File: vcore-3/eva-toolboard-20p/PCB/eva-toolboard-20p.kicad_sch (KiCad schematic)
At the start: 10 parts, among them J1 TH0, J2 HEATER, J3 STEPPER, J4 Main connector, J5 HOTENDFAN, J6 PARTFAN_1, J7 PARTFAN_2, J8 ENDSTOP_X, J9 PROBE

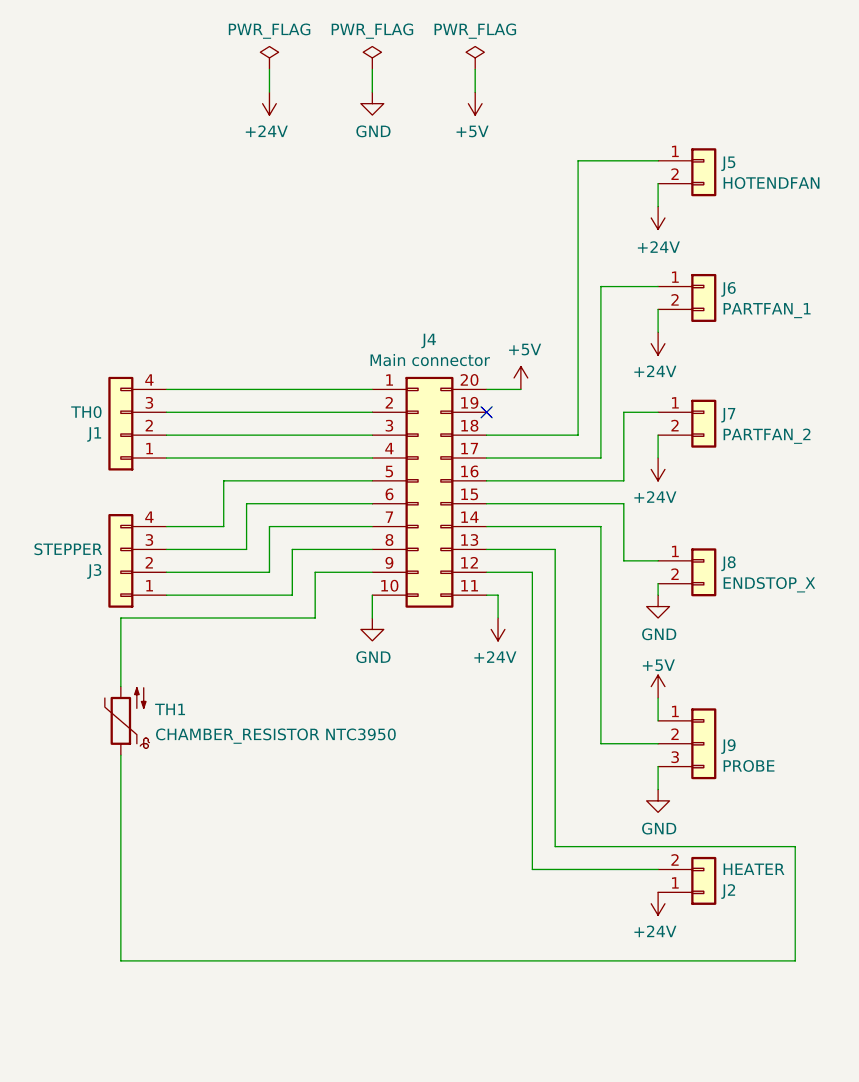
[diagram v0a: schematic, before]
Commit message: Routed PCB and adapted schematic
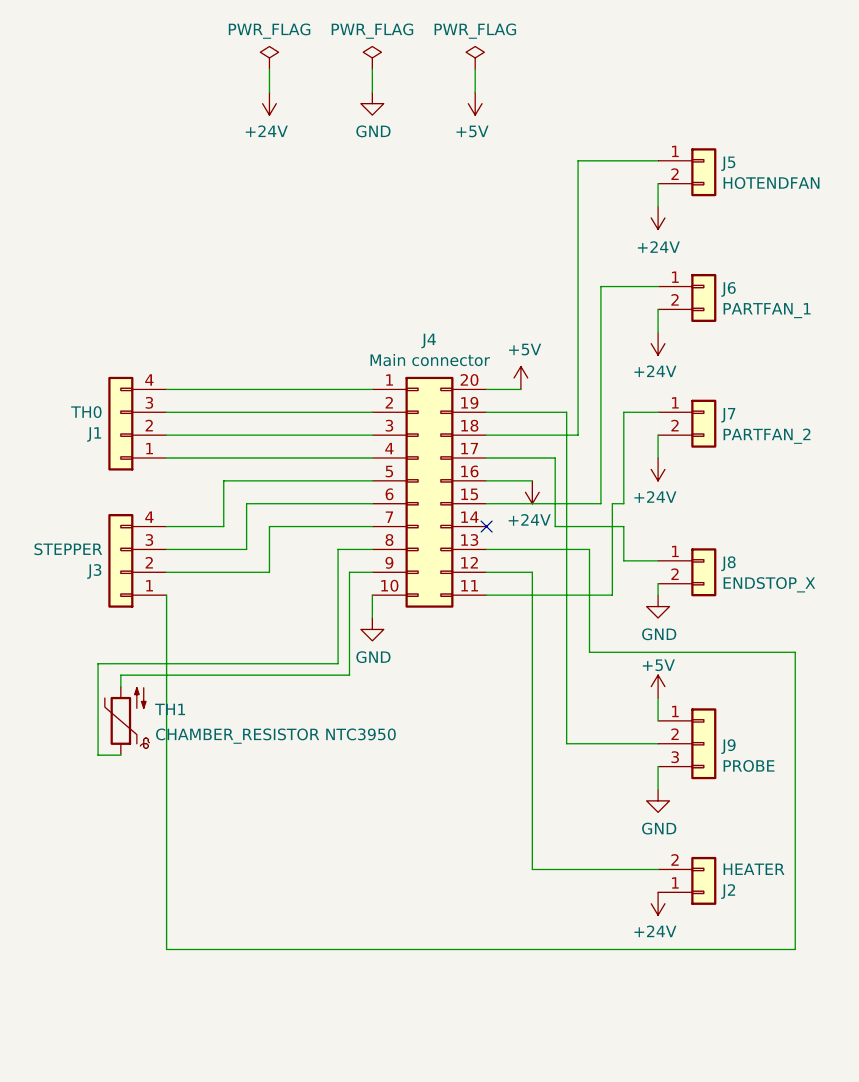
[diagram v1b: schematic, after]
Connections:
- net +24V: now also J4.16 (Pin_16); no longer J4.11 (Pin_11)
- net at J4.13 (Pin_13): now also J3.1 (Pin_1); no longer TH1.1
- net at J4.14 (Pin_14): no longer J9.2 (Pin_2)
- net at J4.15 (Pin_15): now also J6.1 (Pin_1); no longer J8.1 (Pin_1)
- net at J7.1 (Pin_1): now also J4.11 (Pin_11); no longer J4.16 (Pin_16)
- net at J4.17 (Pin_17): now also J8.1 (Pin_1); no longer J6.1 (Pin_1)
- net at J4.19 (Pin_19): now also J9.2 (Pin_2)
- net at J4.8 (Pin_8): now also TH1.1; no longer J3.1 (Pin_1)
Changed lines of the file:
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@@
 (kicad_sch (version 20211123) (generator eeschema)
   (paper "A4")
-  (no_connect (at 147.32 77.47))
+  (no_connect (at 147.32 90.17))
   (wire (pts (xy 111.76 80.01) (xy 134.62 80.01))
     (stroke (width 0) (type default) (color 0 0 0 0))
   )
-  (wire (pts (xy 162.56 93.98) (xy 162.56 87.63))
-    (stroke (width 0) (type default) (color 0 0 0 0))
-  )
-  (wire (pts (xy 160.02 114.3) (xy 166.37 114.3))
+  (wire (pts (xy 132.08 106.68) (xy 132.08 95.25))
+    (stroke (width 0) (type default) (color 0 0 0 0))
+  )
+  (wire (pts (xy 161.29 87.63) (xy 161.29 97.79))
+    (stroke (width 0) (type default) (color 0 0 0 0))
+  )
+  (wire (pts (xy 156.21 114.3) (xy 166.37 114.3))
+    (stroke (width 0) (type default) (color 0 0 0 0))
+  )
+  (wire (pts (xy 130.81 105.41) (xy 104.14 105.41))
+    (stroke (width 0) (type default) (color 0 0 0 0))
+  )
+  (wire (pts (xy 181.61 137.16) (xy 181.61 104.14))
     (stroke (width 0) (type default) (color 0 0 0 0))
   )
@@
     (stroke (width 0) (type default) (color 0 0 0 0))
   )
-  (wire (pts (xy 181.61 138.43) (xy 181.61 125.73))
+  (wire (pts (xy 154.94 82.55) (xy 147.32 82.55))
     (stroke (width 0) (type default) (color 0 0 0 0))
   )
@@
     (stroke (width 0) (type default) (color 0 0 0 0))
   )
+  (wire (pts (xy 147.32 77.47) (xy 156.21 77.47))
+    (stroke (width 0) (type default) (color 0 0 0 0))
+  )
   (wire (pts (xy 166.37 116.84) (xy 166.37 119.38))
     (stroke (width 0) (type default) (color 0 0 0 0))
   )
-  (wire (pts (xy 160.02 90.17) (xy 160.02 114.3))
+  (wire (pts (xy 104.14 105.41) (xy 104.14 115.57))
     (stroke (width 0) (type default) (color 0 0 0 0))
   )
@@
     (stroke (width 0) (type default) (color 0 0 0 0))
   )
-  (wire (pts (xy 154.94 125.73) (xy 154.94 92.71))
-    (stroke (width 0) (type default) (color 0 0 0 0))
-  )
   (wire (pts (xy 123.19 90.17) (xy 134.62 90.17))
     (stroke (width 0) (type default) (color 0 0 0 0))
   )
+  (wire (pts (xy 162.56 93.98) (xy 162.56 90.17))
+    (stroke (width 0) (type default) (color 0 0 0 0))
+  )
   (wire (pts (xy 111.76 92.71) (xy 120.65 92.71))
     (stroke (width 0) (type default) (color 0 0 0 0))
   )
-  (wire (pts (xy 134.62 95.25) (xy 128.27 95.25))
-    (stroke (width 0) (type default) (color 0 0 0 0))
-  )
   (wire (pts (xy 152.4 95.25) (xy 152.4 128.27))
     (stroke (width 0) (type default) (color 0 0 0 0))
@@
     (stroke (width 0) (type default) (color 0 0 0 0))
   )
-  (wire (pts (xy 162.56 85.09) (xy 147.32 85.09))
+  (wire (pts (xy 158.75 104.14) (xy 158.75 92.71))
+    (stroke (width 0) (type default) (color 0 0 0 0))
+  )
+  (wire (pts (xy 160.02 63.5) (xy 160.02 87.63))
     (stroke (width 0) (type default) (color 0 0 0 0))
   )
@@
     (stroke (width 0) (type default) (color 0 0 0 0))
   )
-  (wire (pts (xy 125.73 97.79) (xy 125.73 92.71))
-    (stroke (width 0) (type default) (color 0 0 0 0))
-  )
   (wire (pts (xy 166.37 97.79) (xy 166.37 96.52))
     (stroke (width 0) (type default) (color 0 0 0 0))
@@
     (stroke (width 0) (type default) (color 0 0 0 0))
   )
-  (wire (pts (xy 125.73 92.71) (xy 134.62 92.71))
-    (stroke (width 0) (type default) (color 0 0 0 0))
-  )
   (wire (pts (xy 120.65 92.71) (xy 120.65 87.63))
     (stroke (width 0) (type default) (color 0 0 0 0))
@@
     (stroke (width 0) (type default) (color 0 0 0 0))
   )
-  (wire (pts (xy 162.56 87.63) (xy 147.32 87.63))
-    (stroke (width 0) (type default) (color 0 0 0 0))
-  )
   (wire (pts (xy 134.62 41.91) (xy 134.62 39.37))
     (stroke (width 0) (type default) (color 0 0 0 0))
   )
-  (wire (pts (xy 160.02 82.55) (xy 147.32 82.55))
-    (stroke (width 0) (type default) (color 0 0 0 0))
-  )
-  (wire (pts (xy 147.32 97.79) (xy 148.59 97.79))
+  (wire (pts (xy 161.29 97.79) (xy 147.32 97.79))
+    (stroke (width 0) (type default) (color 0 0 0 0))
+  )
+  (wire (pts (xy 134.62 92.71) (xy 130.81 92.71))
+    (stroke (width 0) (type default) (color 0 0 0 0))
+  )
+  (wire (pts (xy 130.81 92.71) (xy 130.81 105.41))
+    (stroke (width 0) (type default) (color 0 0 0 0))
+  )
+  (wire (pts (xy 111.76 137.16) (xy 181.61 137.16))
+    (stroke (width 0) (type default) (color 0 0 0 0))
+  )
+  (wire (pts (xy 181.61 104.14) (xy 158.75 104.14))
     (stroke (width 0) (type default) (color 0 0 0 0))
   )
@@
     (stroke (width 0) (type default) (color 0 0 0 0))
   )
+  (wire (pts (xy 104.14 115.57) (xy 106.68 115.57))
+    (stroke (width 0) (type default) (color 0 0 0 0))
+  )
   (wire (pts (xy 111.76 74.93) (xy 134.62 74.93))
     (stroke (width 0) (type default) (color 0 0 0 0))
@@
     (stroke (width 0) (type default) (color 0 0 0 0))
   )
-  (wire (pts (xy 128.27 100.33) (xy 106.68 100.33))
-    (stroke (width 0) (type default) (color 0 0 0 0))
-  )
-  (wire (pts (xy 160.02 63.5) (xy 160.02 82.55))
-    (stroke (width 0) (type default) (color 0 0 0 0))
-  )
-  (wire (pts (xy 154.94 92.71) (xy 147.32 92.71))
+  (wire (pts (xy 111.76 97.79) (xy 111.76 137.16))
     (stroke (width 0) (type default) (color 0 0 0 0))
   )
@@
     (stroke (width 0) (type default) (color 0 0 0 0))
   )
-  (wire (pts (xy 162.56 77.47) (xy 162.56 85.09))
+  (wire (pts (xy 162.56 77.47) (xy 162.56 87.63))
     (stroke (width 0) (type default) (color 0 0 0 0))
   )
@@
     (stroke (width 0) (type default) (color 0 0 0 0))
   )
-  (wire (pts (xy 106.68 138.43) (xy 181.61 138.43))
-    (stroke (width 0) (type default) (color 0 0 0 0))
-  )
-  (wire (pts (xy 160.02 90.17) (xy 147.32 90.17))
+  (wire (pts (xy 162.56 90.17) (xy 154.94 90.17))
+    (stroke (width 0) (type default) (color 0 0 0 0))
+  )
+  (wire (pts (xy 106.68 106.68) (xy 132.08 106.68))
+    (stroke (width 0) (type default) (color 0 0 0 0))
+  )
+  (wire (pts (xy 160.02 87.63) (xy 147.32 87.63))
     (stroke (width 0) (type default) (color 0 0 0 0))
   )
@@
     (stroke (width 0) (type default) (color 0 0 0 0))
   )
-  (wire (pts (xy 106.68 115.57) (xy 106.68 138.43))
+  (wire (pts (xy 106.68 107.95) (xy 106.68 106.68))
+    (stroke (width 0) (type default) (color 0 0 0 0))
+  )
+  (wire (pts (xy 154.94 90.17) (xy 154.94 82.55))
     (stroke (width 0) (type default) (color 0 0 0 0))
   )
@@
     (stroke (width 0) (type default) (color 0 0 0 0))
   )
+  (wire (pts (xy 147.32 85.09) (xy 152.4 85.09))
+    (stroke (width 0) (type default) (color 0 0 0 0))
+  )
+  (wire (pts (xy 158.75 92.71) (xy 147.32 92.71))
+    (stroke (width 0) (type default) (color 0 0 0 0))
+  )
   (wire (pts (xy 166.37 68.58) (xy 166.37 66.04))
     (stroke (width 0) (type default) (color 0 0 0 0))
   )
-  (wire (pts (xy 128.27 95.25) (xy 128.27 100.33))
-    (stroke (width 0) (type default) (color 0 0 0 0))
-  )
   (wire (pts (xy 120.65 87.63) (xy 134.62 87.63))
     (stroke (width 0) (type default) (color 0 0 0 0))
@@
     (stroke (width 0) (type default) (color 0 0 0 0))
   )
-  (wire (pts (xy 148.59 100.33) (xy 148.59 97.79))
-    (stroke (width 0) (type default) (color 0 0 0 0))
-  )
-  (wire (pts (xy 106.68 100.33) (xy 106.68 107.95))
-    (stroke (width 0) (type default) (color 0 0 0 0))
-  )
-  (wire (pts (xy 111.76 97.79) (xy 125.73 97.79))
-    (stroke (width 0) (type default) (color 0 0 0 0))
-  )
   (wire (pts (xy 111.76 77.47) (xy 134.62 77.47))
     (stroke (width 0) (type default) (color 0 0 0 0))
@@
     (stroke (width 0) (type default) (color 0 0 0 0))
   )
+  (wire (pts (xy 162.56 87.63) (xy 161.29 87.63))
+    (stroke (width 0) (type default) (color 0 0 0 0))
+  )
   (wire (pts (xy 147.32 74.93) (xy 151.13 74.93))
     (stroke (width 0) (type default) (color 0 0 0 0))
   )
+  (wire (pts (xy 156.21 114.3) (xy 156.21 77.47))
+    (stroke (width 0) (type default) (color 0 0 0 0))
+  )
   (wire (pts (xy 118.11 90.17) (xy 118.11 85.09))
     (stroke (width 0) (type default) (color 0 0 0 0))
   )
+  (wire (pts (xy 132.08 95.25) (xy 134.62 95.25))
+    (stroke (width 0) (type default) (color 0 0 0 0))
+  )
   (wire (pts (xy 123.19 41.91) (xy 123.19 39.37))
-    (stroke (width 0) (type default) (color 0 0 0 0))
-  )
-  (wire (pts (xy 181.61 125.73) (xy 154.94 125.73))
     (stroke (width 0) (type default) (color 0 0 0 0))
   )
@@
     (pin "1")
   )
-  (symbol (lib_id "power:+24V") (at 148.59 100.33 180) (unit 1)
-    (in_bom yes) (on_board yes)
-    (property "Reference" "#PWR03" (id 0) (at 148.59 96.52 0)
-      (effects (font (size 1.27 1.27)) hide)
-    )
-    (property "Value" "+24V" (id 1) (at 148.209 104.7242 0))
-    (property "Footprint" "" (id 2) (at 148.59 100.33 0)
-      (effects (font (size 1.27 1.27)) hide)
-    )
-    (property "Datasheet" "" (id 3) (at 148.59 100.33 0)
-      (effects (font (size 1.27 1.27)) hide)
-    )
+  (symbol (lib_id "power:+24V") (at 152.4 85.09 180) (unit 1)
+    (in_bom yes) (on_board yes)
+    (property "Reference" "#PWR03" (id 0) (at 152.4 81.28 0)
+      (effects (font (size 1.27 1.27)) hide)
+    )
+    (property "Value" "+24V" (id 1) (at 152.019 89.4842 0))
+    (property "Footprint" "" (id 2) (at 152.4 85.09 0)
+      (effects (font (size 1.27 1.27)) hide)
+    )
+    (property "Datasheet" "" (id 3) (at 152.4 85.09 0)
+      (effects (font (size 1.27 1.27)) hide)
+    )
